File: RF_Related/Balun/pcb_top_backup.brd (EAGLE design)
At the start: 39 x 30 mm, 4 parts, among them T1 ADT1-1WT+, X1 SMA-142-0701-801/806, X2 SMA-142-0701-801/806, X3 SMA-142-0701-801/806

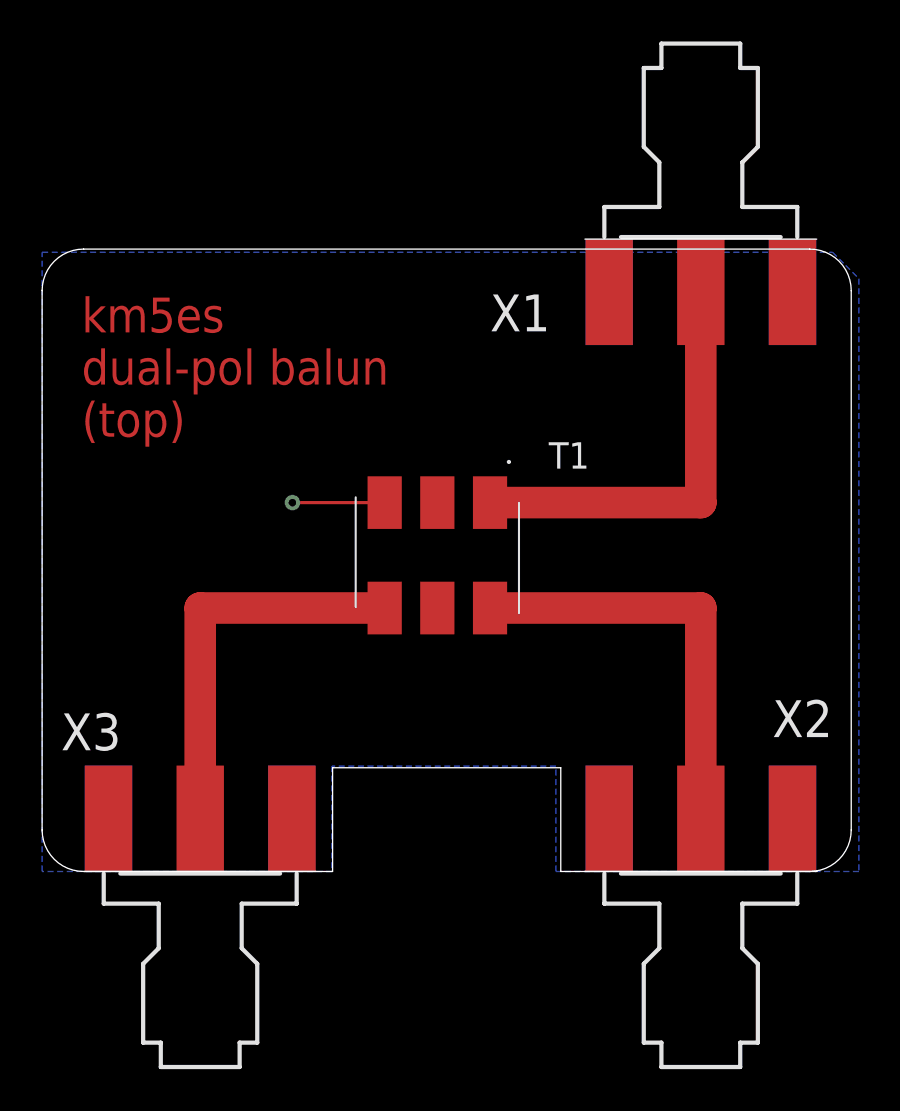
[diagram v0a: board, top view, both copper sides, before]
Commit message: balun is ready. do final checks on other boards before sending them in. 3D model of drone now has GPSDO antenna and more in the payload.
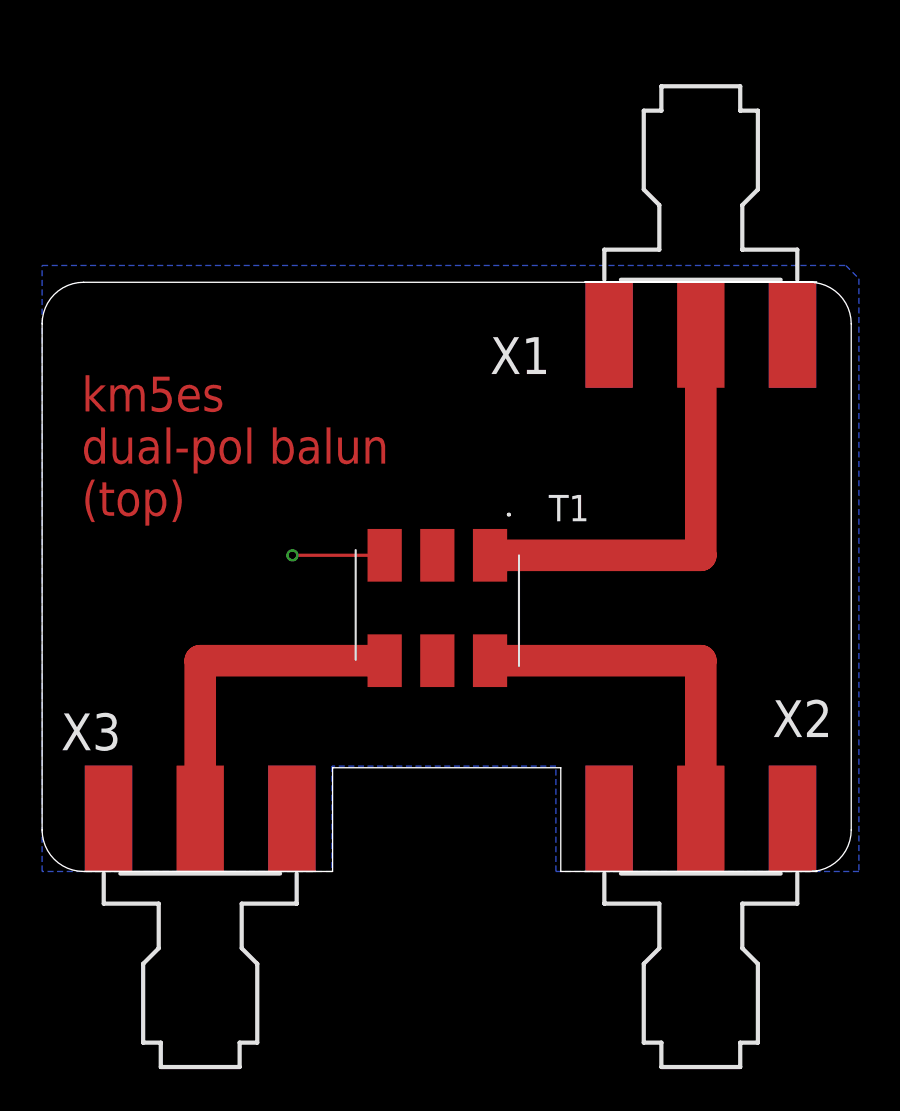
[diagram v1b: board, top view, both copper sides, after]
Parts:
- moved T1 2.54 mm to (19.1, 12.7)
- moved X1 2.06 mm to (31.8, 28.4)
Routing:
- net N$3: track 19.0 -> 16.5 mm
- net N$2: track 19.7 -> 17.1 mm
- net N$1: track 19.7 -> 20.8 mm
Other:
- board size 39 x 30 mm -> 39 x 28.4 mm

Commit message: doing a second revision of balun boards. going to do another rev of the payload bays soon.
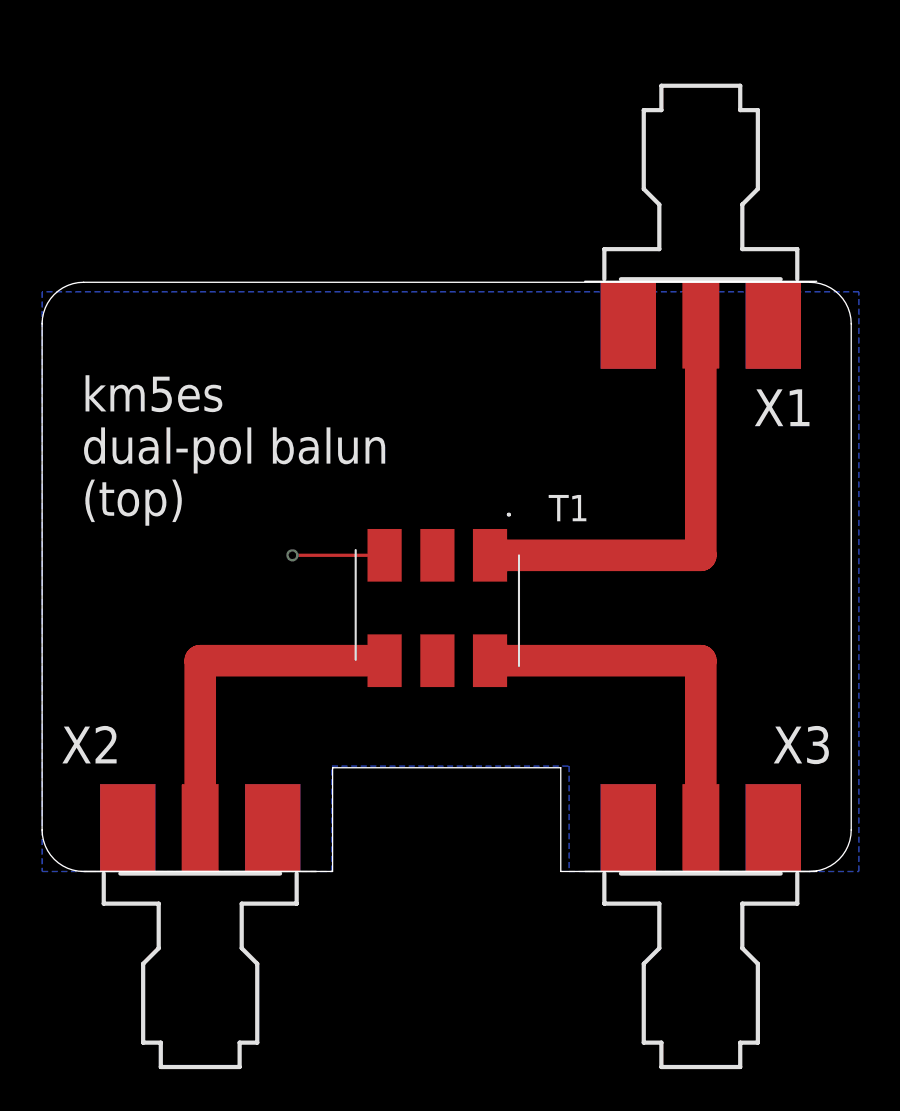
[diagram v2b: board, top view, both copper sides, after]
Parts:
- X1, X2, X3: value SMA-142-0701-801/806 -> SMA-142-0711-821/826; device con-coax:J502-ND-142-0701-801/806 -> con-coax:J502-ND-142-0711-821/826
- moved X2 24.1 mm to (7.62, 0.00)
- moved X3 24.1 mm to (31.8, 0.00)
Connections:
- net N$2: now also X3.1; no longer X2.1
- net N$3: now also X2.1; no longer X3.1
